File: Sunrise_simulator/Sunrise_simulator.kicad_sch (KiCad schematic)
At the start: 14 parts, among them J1 Jack-DC, J2 SD_Card_Device, SW1 Switch ON-OFF, SW2 BUTTON_PLUS, SW3 BUTTON_MINUS, SW4 BUTTON_VALIDATE, SW5 BUTTON_PARAMETER, U1 MP1584EN, U2 MAX98357A, U3 E-ink display

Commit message: ajout ecran
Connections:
- net BUTTON_MINUS_PIN: now also ESP32devkitV1.3 (D2); no longer ESP32devkitV1.28 (D16)
- net BUTTON_PLUS_PIN: now also ESP32devkitV1.27 (D15); no longer ESP32devkitV1.18 (D4)
- net BUTTON_VALIDATE_PIN: now also ESP32devkitV1.18 (D4); no longer ESP32devkitV1.19 (D17)
- net DISPLAY_BUSY: now also ESP32devkitV1.26 (D22); no longer ESP32devkitV1.21 (D18)
- net DISPLAY_CS: now also ESP32devkitV1.20 (D5); no longer ESP32devkitV1.24 (D0/RX)
- net LIGHT_PIN: now also ESP32devkitV1.19 (D17); no longer ESP32devkitV1.16 (D23)
- net SD_CLK: no longer J2.5 (CLK)
- net SD_MOSI: no longer J2.1 (MOSI)
- net SWITCH_LIGHT_PIN: now also ESP32devkitV1.28 (D16); no longer ESP32devkitV1.20 (D5)
- net DISPLAY_SCL: no longer names the net of ESP32devkitV1.25 (D1/TX)
- net DISPLAY_SCL: no longer U3.20 (SCL)
- net DISPLAY_SDA renamed SDA
- net SDA: now also ESP32devkitV1.16 (D23), J2.1 (MOSI); no longer ESP32devkitV1.26 (D22)
- new net SCL: ESP32devkitV1.21 (D18), J2.5 (CLK), U3.20 (SCL)

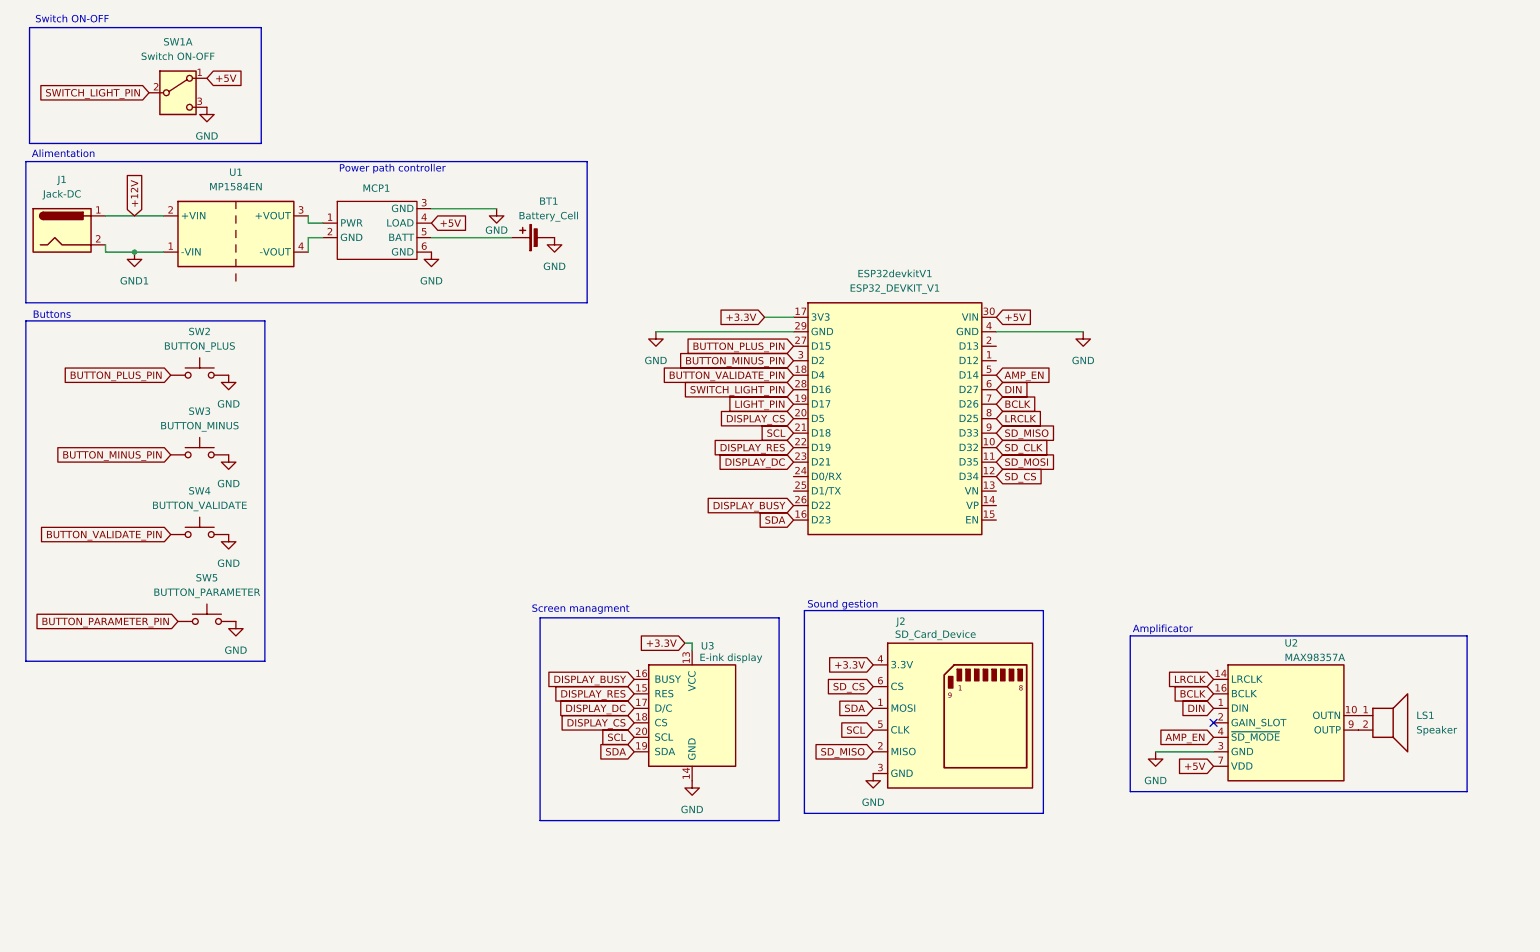
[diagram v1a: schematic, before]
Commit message: ajout de la gestion RTC + rétroéclairage + front plate
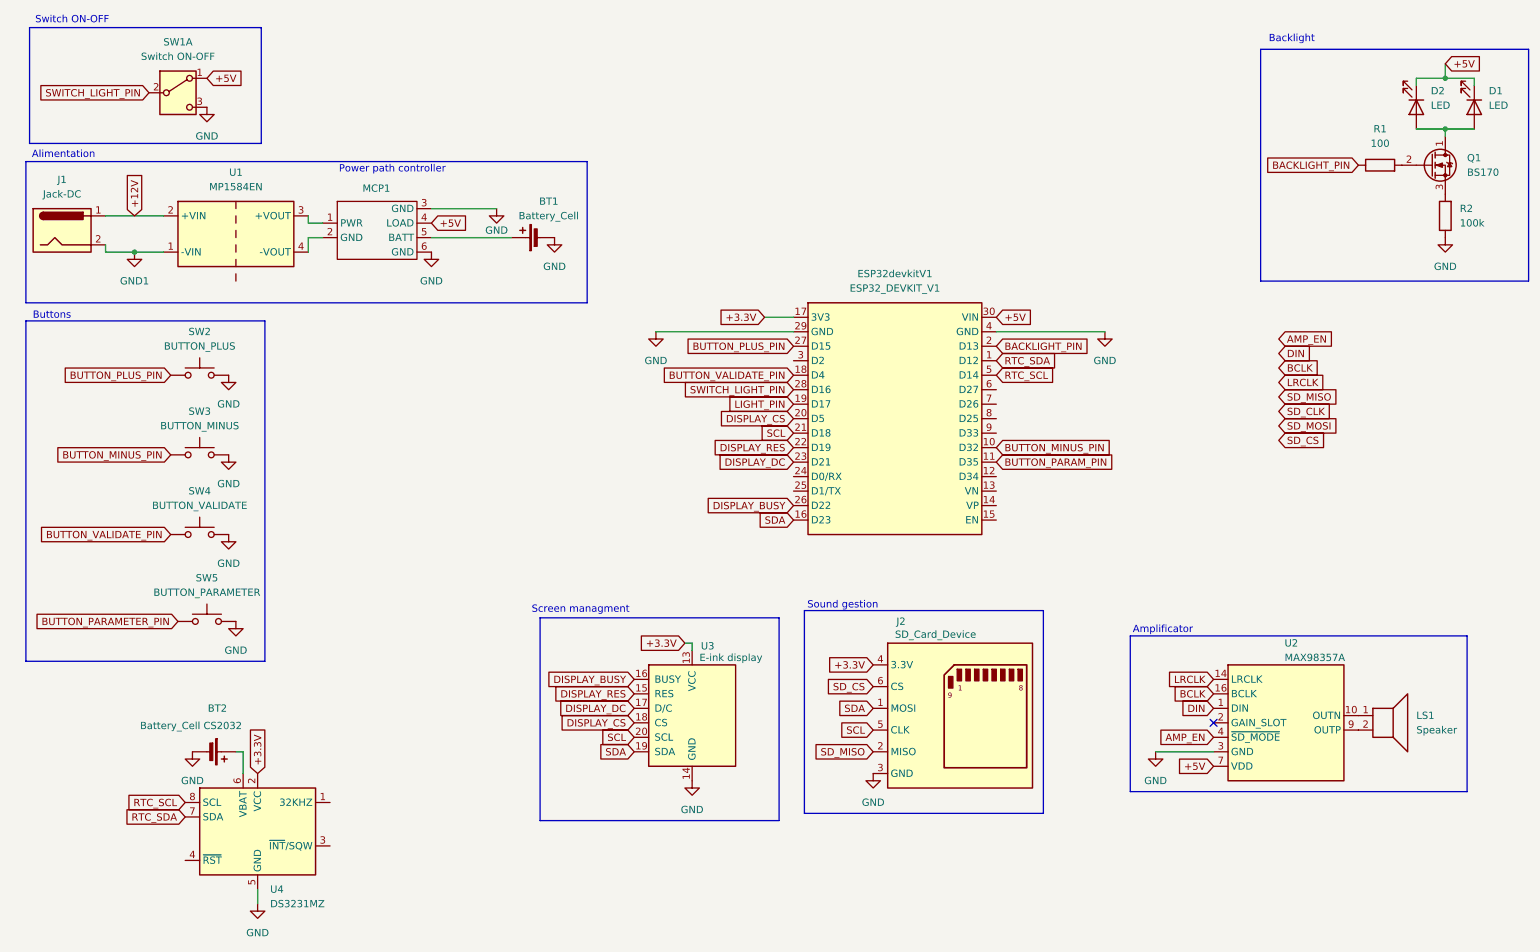
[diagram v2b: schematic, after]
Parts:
- added BT2: Battery_Cell CS2032, symbol Device:Battery_Cell
- added D1, D2: LED, symbol Device:LED
- added Q1: BS170, Package_TO_SOT_THT:TO-92_Inline, symbol Transistor_FET:BS170
- added R1: 100, symbol Device:R
- added R2: 100k, symbol Device:R
- added U4: DS3231MZ, Package_SO:SOIC-8_3.9x4.9mm_P1.27mm, symbol Timer_RTC:DS3231MZ
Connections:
- net +3.3V: now also U4.2 (VCC)
- net +5V: now also D1.1 (K), D2.1 (K)
- net AMP_EN: no longer ESP32devkitV1.5 (D14)
- net BCLK: no longer ESP32devkitV1.7 (D26)
- net BUTTON_MINUS_PIN: now also ESP32devkitV1.10 (D32); no longer ESP32devkitV1.3 (D2)
- net DIN: no longer ESP32devkitV1.6 (D27)
- net GND: now also BT2.2 (-), R2.1, U4.5 (GND)
- net LRCLK: no longer ESP32devkitV1.8 (D25)
- net SD_CLK: no longer ESP32devkitV1.10 (D32)
- net SD_CS: no longer ESP32devkitV1.12 (D34)
- net SD_MISO: no longer ESP32devkitV1.9 (D33)
- net SD_MOSI: no longer ESP32devkitV1.11 (D35)
- net RTC_SDA: now reaches ESP32devkitV1.1 (D12)
- net RTC_SDA: now also U4.7 (SDA)
- net BACKLIGHT_PIN: now reaches ESP32devkitV1.2 (D13)
- net BACKLIGHT_PIN: now also R1.1
- new net: BT2.1 (+), U4.6 (VBAT)
- new net: D1.2 (A), D2.2 (A), Q1.1 (D)
- new net: Q1.2 (G), R1.2
- new net: Q1.3 (S), R2.2
- new net BUTTON_PARAM_PIN: ESP32devkitV1.11 (D35)
- new net RTC_SCL: ESP32devkitV1.5 (D14), U4.8 (SCL)
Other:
- note added: "Backlight"

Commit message: update kicad schematic
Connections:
- net AMP_EN: now also ESP32devkitV1.8 (D25)
- net BCLK: now also ESP32devkitV1.12 (D34)
- net BUTTON_PARAM_PIN: now also ESP32devkitV1.9 (D33); no longer ESP32devkitV1.11 (D35)
- net DIN: now also ESP32devkitV1.1 (D12)
- net LRCLK: now also ESP32devkitV1.7 (D26)
- net RTC_SDA: now also ESP32devkitV1.6 (D27); no longer ESP32devkitV1.1 (D12)
- net SD_CS: now also ESP32devkitV1.3 (D2)
- net SD_MISO: now also ESP32devkitV1.11 (D35)

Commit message: ajout sonnerie + big refacto
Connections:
- net BCLK: now also ESP32devkitV1.1 (D12); no longer ESP32devkitV1.12 (D34)
- net DIN: now also ESP32devkitV1.25 (D1/TX); no longer ESP32devkitV1.1 (D12)
